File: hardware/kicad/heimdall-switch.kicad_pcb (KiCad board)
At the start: 2 copper layers, 95.8 x 23 mm, 42 parts, among them J1 SWD (ARM 10-pin), J2 LOAD_OUT, J3 BATT_IN, J4 B3B-XH-A, Q1 AO3400A, Q2 BSS84, Q3 AO4407A, Q4 AO4407A, Q5 AO3400A, Q6 BSS84, SW1 KSC641J, U1 BT832, U2 TPS629206, Y1 32.768kHz

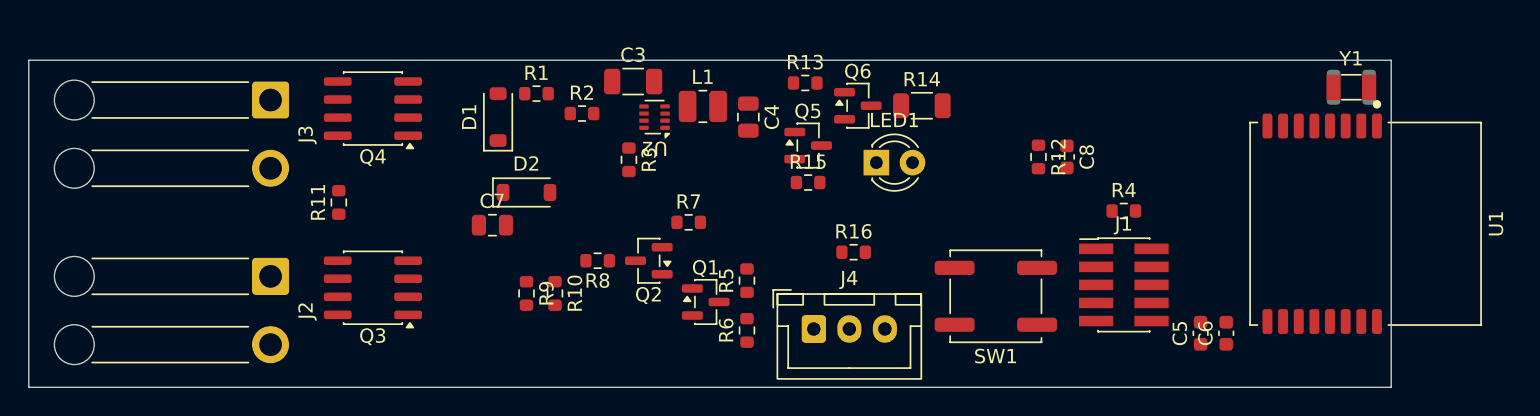
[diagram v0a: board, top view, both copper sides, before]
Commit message: Main PCB placement iteration 2: two-sided, 71.8 x 23 mm
Small parts (regulator, gate networks, LED driver, decoupling, crystal
load caps) on the bottom; wires, power FETs, BT832, crystal, headers,
button and LED on top. No courtyard overlaps, full schematic parity.

Co-Authored-By: Claude Opus 5.5 <noreply@anthropic.com>
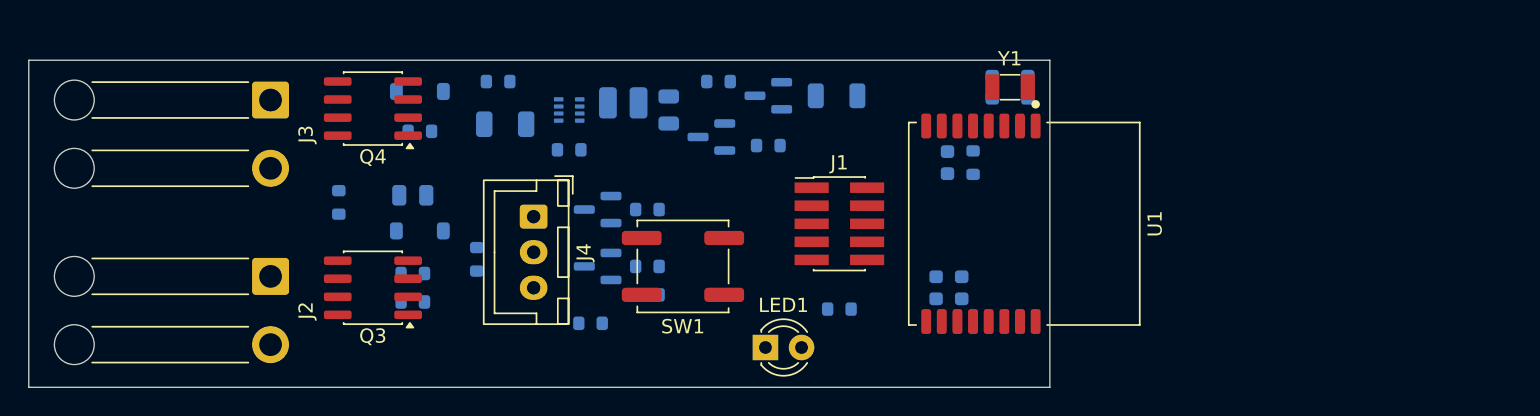
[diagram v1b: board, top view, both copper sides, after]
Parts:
- C3, C4, C5, C6, C7, C8, D1, D2, L1, Q1, Q2, Q5, Q6, R1, R10, R11, R12, R13, R14, R15, R16, R2, R3, R4, R5, R6, R7, R8, R9, U2: moved to B.Cu
- moved C1 24.0 mm to (170.2, 101.9)
- moved C2 24.0 mm to (167.8, 101.9)
- moved U1 24.0 mm to (170.0, 111.5)
- moved Y1 24.0 mm to (169.0, 101.9)
- moved SW1 22.1 mm to (146.0, 114.5)
- moved J4 21.2 mm to (135.5, 111.0), turned to -90 degrees
- moved R4 21.2 mm to (157.0, 117.5), turned to 180 degrees
- moved J1 20.5 mm to (157.0, 111.5)
- moved R16 19.2 mm to (139.5, 118.5), turned to 180 degrees
- moved C5 18.9 mm to (163.8, 116.0)
- moved C6 18.9 mm to (165.6, 116.0)
- moved LED1 15.2 mm to (151.8, 120.2)
- moved R10 10.0 mm to (127.0, 117.0), turned to 180 degrees
- moved C3 9.49 mm to (133.5, 104.5), turned to 180 degrees
- moved R1 8.62 mm to (127.5, 105.0), turned to 180 degrees
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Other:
- board size 95.8 x 23 mm -> 71.8 x 23 mm

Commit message: Main board SW1: small C&K PTS810 (4.2x3.2mm), placed next to LED1
The sealed KSC641J stays on the daughter board, which sits outside the
hull; the on-board button is inside, so a small unsealed part is fine.

Co-Authored-By: Claude Opus 5.5 <noreply@anthropic.com>
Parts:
- SW1: value KSC641J -> PTS810; footprint Button_Switch_SMD:SW_Push_1P1T_NO_CK_KSC6xxJ -> Button_Switch_SMD:SW_SPST_PTS810
- moved SW1 5.12 mm to (146.4, 119.6)

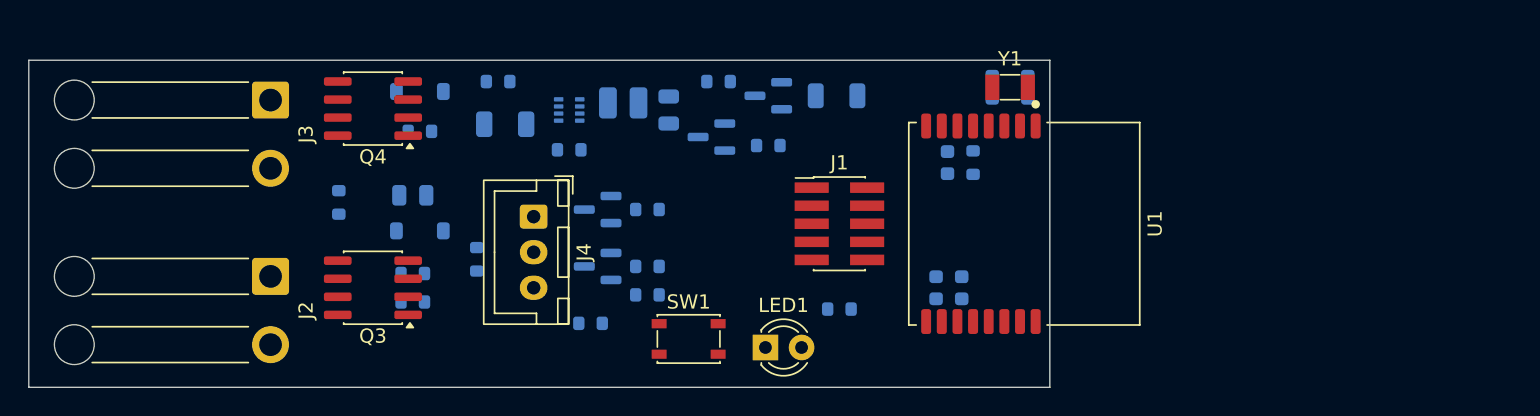
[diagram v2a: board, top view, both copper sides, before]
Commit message: Main PCB placement iteration 3: BT832 mid-board, 63.5 x 23 mm
U1 at native orientation in the middle, antenna over a 15 x 6.3 mm
notch cut into the top edge (no board or copper under it, per Fanstel).
Left pin column (crystal, ADC, LED) faces the power/regulator half,
right column (debug, button, VDD) faces J4. J1 on the back under the
module body; SW1/LED1 in the strip below it. No courtyard overlaps,
full schematic parity. placement-top/bottom.png show the ratsnest.

Co-Authored-By: Claude Opus 5.5 <noreply@anthropic.com>
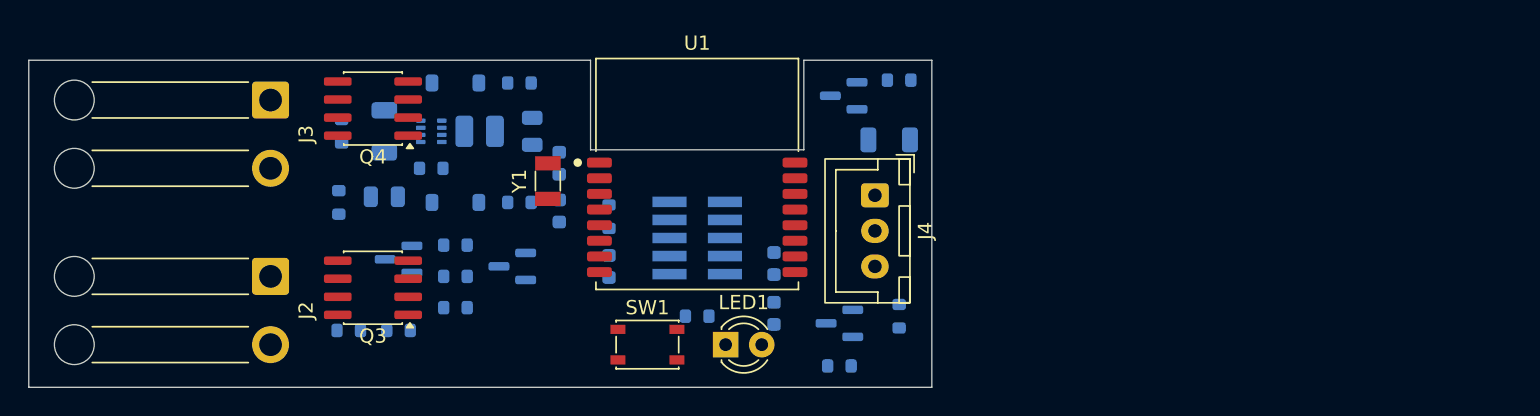
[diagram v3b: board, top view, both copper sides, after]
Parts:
- J1: moved to B.Cu
- moved C1 33.4 mm to (137.3, 107.2)
- moved Y1 33.2 mm to (136.5, 108.5), turned to 90 degrees
- moved C2 31.7 mm to (137.3, 110.6)
- moved R12 25.9 mm to (140.8, 111.0)
- moved C8 24.9 mm to (140.8, 114.5)
- moved J4 24.0 mm to (159.5, 109.5)
- moved U1 23.3 mm to (147.0, 108.0), turned to 0 degrees
- moved R16 17.8 mm to (157.0, 121.5)
- moved Q5 15.9 mm to (157.0, 118.5)
- moved R15 15.1 mm to (161.2, 118.0), turned to 90 degrees
- moved Q2 14.4 mm to (126.0, 114.0)
- moved R7 13.7 mm to (130.0, 113.0)
- moved R6 13.5 mm to (130.0, 117.4)
- moved R5 13.5 mm to (130.0, 115.2)
- moved C6 13.3 mm to (152.4, 114.3)
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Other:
- board size 71.8 x 23 mm -> 63.5 x 23 mm

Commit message: Main PCB: readable silkscreen, spread the bottom cluster
- Every reference designator on silk at 0.8mm (JLCPCB minimum), placed
  next to its own part and clear of pads, holes, other labels and the
  board edge (silk_labels.py, scored so labels aren't ambiguous);
  values moved to the fab layer
- Bottom left section re-gridded into five rows with label space;
  regulator chain R2/C3 -> U2 -> L1 -> C4 kept in one line
- BT832 footprint: no silk over the antenna (it now sits over the notch)

DRC: 0 violations, full schematic parity (only unrouted remains).

Co-Authored-By: Claude Opus 5.5 <noreply@anthropic.com>
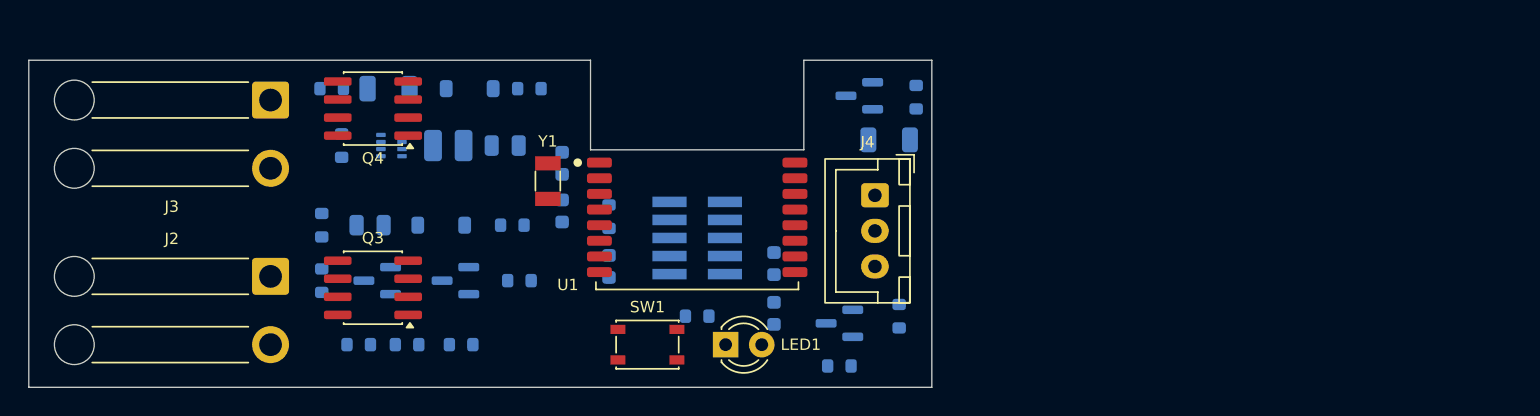
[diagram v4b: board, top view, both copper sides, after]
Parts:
- moved R8 14.9 mm to (120.6, 115.5), turned to 90 degrees
- moved R3 6.50 mm to (122.0, 106.0), turned to 90 degrees
- moved R5 4.51 mm to (134.5, 115.5)
- moved R7 4.24 mm to (134.0, 111.6)
- moved Q1 4.12 mm to (130.0, 115.5)
- moved R2 3.08 mm to (121.3, 102.0), turned to 180 degrees
- moved C3 3.01 mm to (125.3, 102.0), turned to 180 degrees
- moved U2 2.97 mm to (125.5, 106.0)
- moved R6 2.63 mm to (130.4, 120.0)
- moved L1 2.42 mm to (129.5, 106.0)
- moved C7 2.24 mm to (124.0, 111.6)
- moved C4 2.15 mm to (133.5, 106.0), turned to 180 degrees
- moved Q2 2.12 mm to (124.5, 115.5)
- moved R11 2.00 mm to (120.6, 111.6)
- moved D2 1.89 mm to (129.0, 111.6)
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
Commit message: Main PCB: first full routing (63.5 x 23 mm, 2 layers, DRC clean)
- 3A path as solid top copper (BATT+, VBAT bar, LOAD) with track
  keep-outs so nothing can split it; gate stubs to vias
- GND pours both layers with stitching; solid GND on the wire pads
- No top copper under the BT832 body (unused LGA pads)
- Net classes Power/Reg/Default + neck-down rule for fine-pitch pads
- Routed with Freerouting via route_pcb.py (prep/finish/stitch/cleanup);
  39 vias, ~630 mm of track
- Placement tweaks for routability: LED driver to the top next to the
  VBAT bar, regulator loop tightened (L1/C4/C3/R3 orientation), R15/R16
  rotated

DRC: 0 violations, 0 unconnected, full schematic parity.

Co-Authored-By: Claude Opus 5.5 <noreply@anthropic.com>
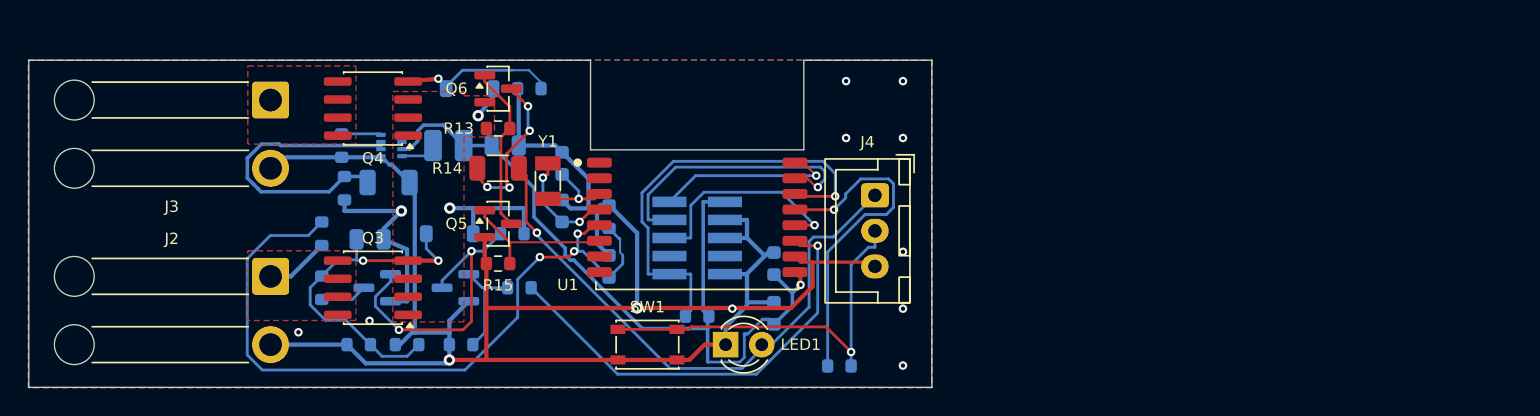
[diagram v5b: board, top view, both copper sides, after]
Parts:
- Q5, Q6, R13, R14, R15: moved to F.Cu
- moved R13 29.5 mm to (133.0, 104.8), turned to 0 degrees
- moved R15 28.4 mm to (133.0, 114.3), turned to 180 degrees
- moved R14 27.6 mm to (133.0, 107.6), turned to 0 degrees
- moved Q6 25.4 mm to (133.0, 102.0), turned to 0 degrees
- moved Q5 25.0 mm to (133.0, 111.5), turned to 0 degrees
- moved R2 7.06 mm to (122.2, 109.0), turned to 90 degrees
- moved C3 6.60 mm to (125.3, 108.6), turned to 0 degrees
- moved C7 1.00 mm to (124.0, 112.6)
- moved D2 0.85 mm to (129.6, 112.2)
- moved R11 0.60 mm to (120.6, 112.2)
- moved R7 0.60 mm to (134.0, 112.2)
- moved Q1 0.50 mm to (130.0, 116.0)
- moved Q2 0.50 mm to (124.5, 116.0)
- moved R5 0.50 mm to (134.5, 116.0)
- moved R8 0.50 mm to (120.6, 116.0)
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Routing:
- net GND: track 0.00 -> 148.6 mm, vias 0 -> 12
- net +3V3: track 0.00 -> 56.4 mm, vias 0 -> 1
- net /ADC_FB: track 0.00 -> 52.0 mm, vias 0 -> 3
- net /LED_A: track 0.00 -> 40.8 mm, vias 0 -> 1
- net /nRESET: track 0.00 -> 31.4 mm, vias 0 -> 1
- net /OUT_OFF: track 0.00 -> 30.9 mm, vias 0 -> 1
- net Net-(J4-Pin_2): track 0.00 -> 27.7 mm, vias 0 -> 1
- net VBAT: track 0.00 -> 25.0 mm, vias 0 -> 3
- net /Q3_GATE: track 0.00 -> 24.2 mm, vias 0 -> 2
- net /BTN: track 0.00 -> 23.7 mm, vias 0 -> 1
- net Net-(U2-EN): track 0.00 -> 21.3 mm
- net Net-(Q1-D): track 0.00 -> 21.3 mm, vias 0 -> 2
- net /SWDCLK: track 0.00 -> 19.8 mm, vias 0 -> 1
- net /SWO: track 0.00 -> 15.2 mm, vias 0 -> 1
- net /SWDIO: track 0.00 -> 13.0 mm, vias 0 -> 1
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- added copper zone on F.Cu, net /BATT+
- added copper zone on F.Cu, net /LOAD_OUT
- added copper zone on B.Cu, net GND
- added copper zone on F.Cu, net GND
- added copper zone on F.Cu, net VBAT

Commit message: Main PCB: J1 to the top, widen the VBAT bar for servo stall currents
- J1 (debug header) moved to the top at the right end, above J4: the
  bottom side now carries only flat SMD parts
- VBAT bar widened to ~7mm into the copper under Q3/Q4; Q3's gate now
  leaves through a via right above its pad instead of a stub across the
  bar (the old stub left ~1.3mm of copper in the load path)
- Q2's VBAT fed from its own via in the bar
- Documented expected servo stall currents and the copper capacity
  (5A continuous / 15A peaks target; ~8-10A continuous on 1oz)
- Re-routed: 30 vias, DRC 0 violations, 0 unconnected, full parity

Co-Authored-By: Claude Opus 5.5 <noreply@anthropic.com>
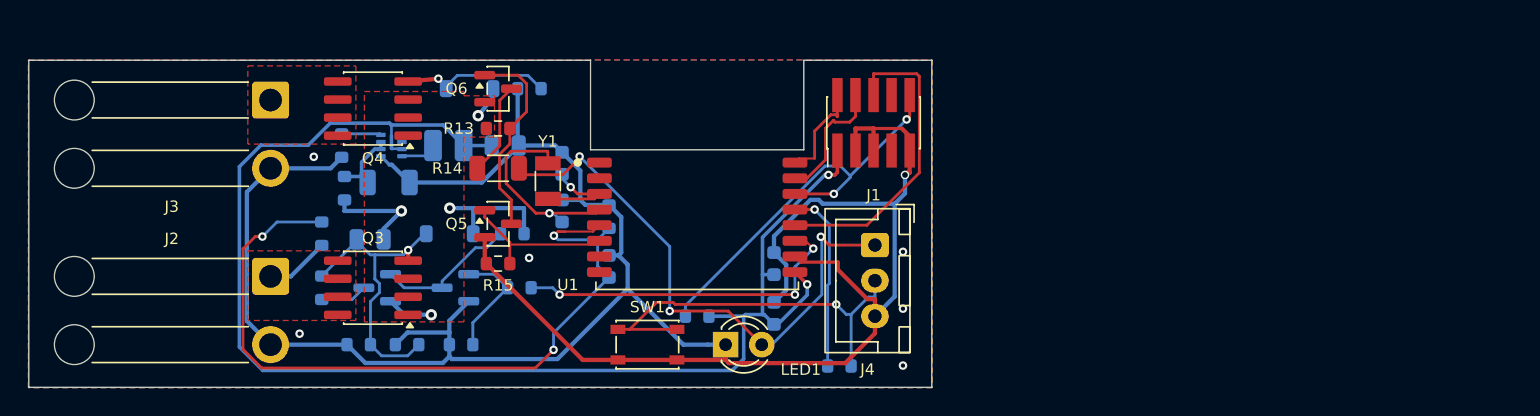
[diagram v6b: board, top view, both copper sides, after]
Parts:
- J1: moved to F.Cu
- moved J1 14.8 mm to (159.4, 104.4), turned to 90 degrees
- moved J4 3.50 mm to (159.5, 113.0)
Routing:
- net +3V3: track 56.4 -> 99.2 mm, vias 1 -> 2
- net GND: track 148.6 -> 177.1 mm, vias 12 -> 7
- net Net-(U2-EN): track 21.3 -> 5.05 mm
- net Net-(Q1-D): track 21.3 -> 9.98 mm, vias 2 -> 0
- net /BTN: track 23.7 -> 12.9 mm
- net /SWDCLK: track 19.8 -> 8.95 mm, vias 1 -> 0
- net /OUT_OFF: track 30.9 -> 24.0 mm, vias 1 -> 3
- net /SWO: track 15.2 -> 21.9 mm, vias 1 -> 0
- net Net-(U1-P0.01_XL2): track 7.90 -> 14.5 mm, vias 2 -> 1
- net /SWDIO: track 13.0 -> 7.06 mm, vias 1 -> 0
- net Net-(Q6-D): track 11.4 -> 6.59 mm, vias 4 -> 0
- net VBAT: track 25.0 -> 21.6 mm, vias 3 -> 4
- net /Q3_GATE: track 24.2 -> 21.0 mm, vias 2 -> 1
- net /nRESET: track 31.4 -> 28.6 mm, vias 1 -> 2
- net Net-(Q5-D): track 11.7 -> 14.2 mm
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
